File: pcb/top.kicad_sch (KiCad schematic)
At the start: 78 parts, among them J1 Conn_01x01, J10 Conn_01x01, J11 Conn_01x01, J2 Conn_01x01, J3 Conn_01x06, J4 Conn_01x01, J5 Conn_01x01, J6 Conn_01x01, J7 Conn_01x01, J8 Conn_01x01, J9 Conn_01x01, Q1 2N7002, Q2 2N7002, Q3 2N7002, Q4 2N7002, U1 L78L05_SOT89, U2 PIC12F629-ISN, U3 L78L08_SOT89

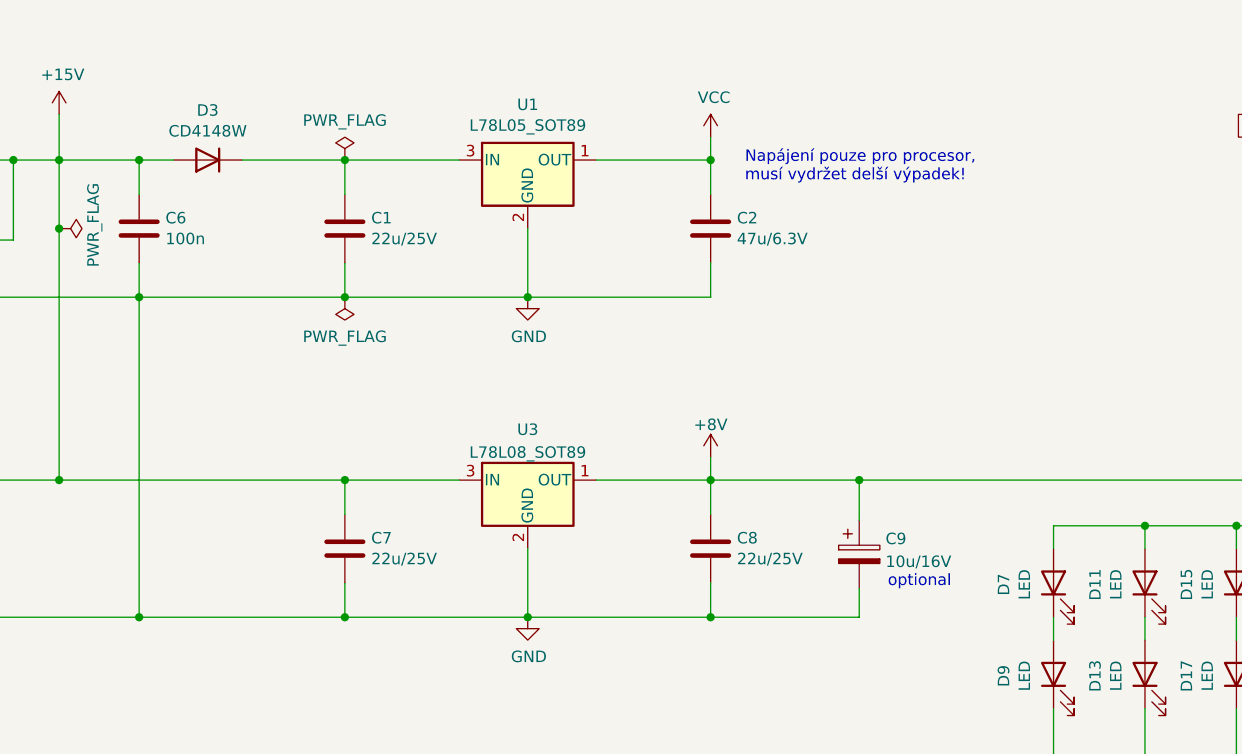
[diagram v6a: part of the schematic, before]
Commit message: Use 1N5819 insteas on 1N4148.
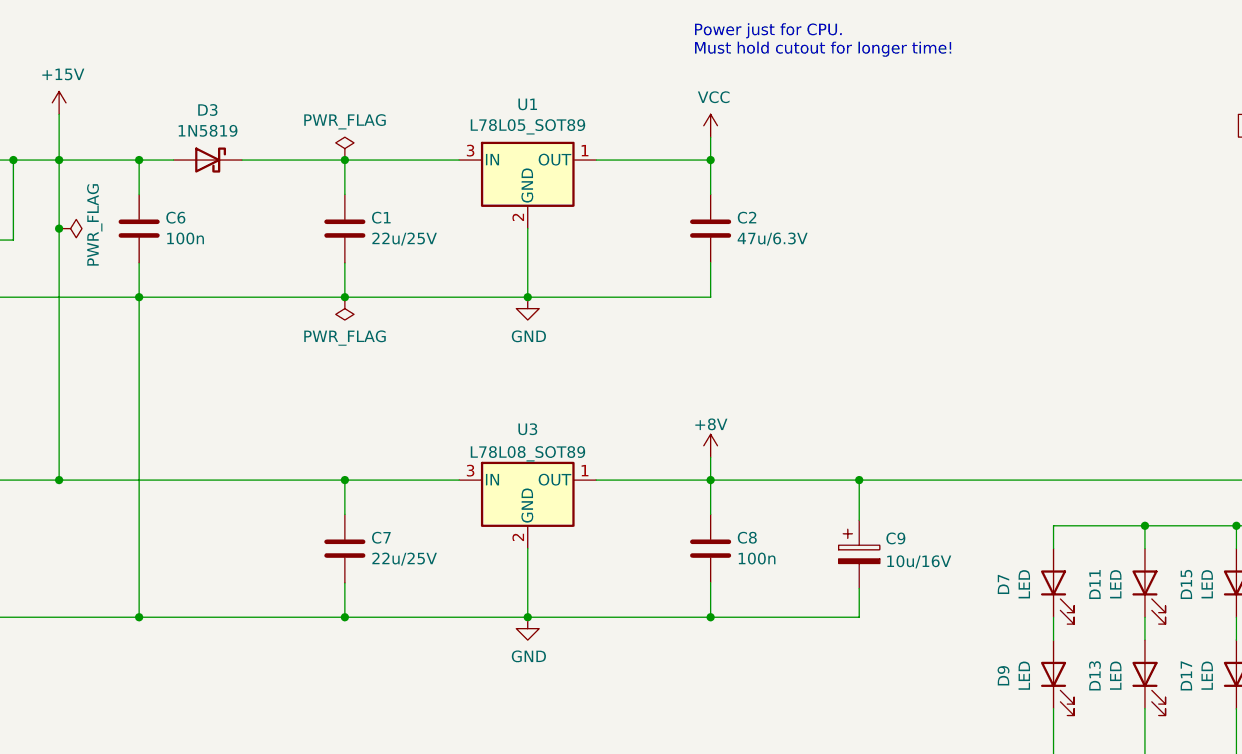
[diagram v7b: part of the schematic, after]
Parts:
- removed D3: CD4148W, Diode_SMD:D_0805_2012Metric_Pad1.15x1.40mm_HandSolder, symbol Diode:CD4148W
- added D3: 1N5819, Diode_SMD:D_SOD-123, symbol Diode:1N5819
- C8: value 22u/25V -> 100n; LCSC C45783 -> C49678
- C9: JLCPCB_IGNORE true -> (none); LCSC (none) -> C7171
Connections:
- net +15V: now also D3.2 (A)
- net at C1.1, U1.3 (IN): now also D3.1 (K)
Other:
- note added: "Power just for CPU. Must hold cutout for longer time!"
- note removed: "Napájení pouze pro procesor, musí vydržet delší výpadek!"
- note removed: "optional"
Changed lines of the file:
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@@
     (stroke (width 0) (type default) (color 0 0 0 0))
   )
-  (text "Napájení pouze pro procesor,\nmusí vydržet delší výpadek!"
-    (at 160.02 39.37 0)
+  (text "Power just for CPU.\nMust hold cutout for longer time!"
+    (at 154.305 25.4 0)
     (effects (font (size 1.27 1.27)) (justify left bottom))
   )
@@
   )
   (text "Programming\nconnector" (at 233.68 29.21 0)
-    (effects (font (size 1.27 1.27)) (justify left bottom))
-  )
-  (text "optional" (at 175.895 84.455 0)
     (effects (font (size 1.27 1.27)) (justify left bottom))
   )
@@
     (pin "2")
   )
-  (symbol (lib_id "Diode:CD4148W") (at 100.33 36.83 180) (unit 1)
-    (in_bom yes) (on_board yes)
-    (property "Reference" "D3" (id 0) (at 100.33 31.3182 0))
-    (property "Value" "CD4148W" (id 1) (at 100.33 33.6296 0))
-    (property "Footprint" "Diode_SMD:D_0805_2012Metric_Pad1.15x1.40mm_HandSolder" (id 2) (at 100.33 31.75 0)
-      (effects (font (size 1.27 1.27)) hide)
-    )
-    (property "Datasheet" "https://www.dccomponents.com/upload/product/original/806236332588.pdf" (id 3) (at 100.33 36.83 0)
-      (effects (font (size 1.27 1.27)) hide)
-    )
-    (property "LCSC" "C2128" (id 4) (at 100.33 36.83 0)
-      (effects (font (size 1.27 1.27)) hide)
-    )
-    (pin "1")
-    (pin "2")
-  )
   (symbol (lib_id "Diode:1N5819") (at 67.31 72.39 0) (mirror y) (unit 1)
     (in_bom yes) (on_board yes)
@@
       (effects (font (size 1.27 1.27)) hide)
     )
-    (property "JLCPCB_IGNORE" "true" (id 4) (at 172.72 80.645 0)
+    (property "LCSC" "C7171" (id 5) (at 172.72 80.645 0)
       (effects (font (size 1.27 1.27)) hide)
     )
@@
       (effects (font (size 1.27 1.27)) (justify left))
     )
-    (property "Value" "22u/25V" (id 1) (at 159.131 81.153 0)
+    (property "Value" "100n" (id 1) (at 159.131 81.153 0)
       (effects (font (size 1.27 1.27)) (justify left))
     )
@@
       (effects (font (size 1.27 1.27)) hide)
     )
-    (property "LCSC" "C45783" (id 4) (at 156.21 80.01 0)
+    (property "LCSC" "C49678" (id 4) (at 156.21 80.01 0)
       (effects (font (size 1.27 1.27)) hide)
     )
@@
     (pin "1")
   )
+  (symbol (lib_id "Diode:1N5819") (at 100.33 36.83 0) (mirror y) (unit 1)
+    (in_bom yes) (on_board yes)
+    (property "Reference" "D3" (id 0) (at 100.33 31.3182 0))
+    (property "Value" "1N5819" (id 1) (at 100.33 33.6296 0))
+    (property "Footprint" "Diode_SMD:D_SOD-123" (id 2) (at 100.33 41.275 0)
+      (effects (font (size 1.27 1.27)) hide)
+    )
+    (property "Datasheet" "http://www.vishay.com/docs/88525/1n5817.pdf" (id 3) (at 100.33 36.83 0)
+      (effects (font (size 1.27 1.27)) hide)
+    )
+    (property "LCSC" "C8598" (id 4) (at 100.33 36.83 0)
+      (effects (font (size 1.27 1.27)) hide)
+    )
+    (pin "1")
+    (pin "2")
+  )
   (symbol (lib_id "power:+15V") (at 261.62 110.49 0) (unit 1)
     (in_bom yes) (on_board yes)
@@
     )
     (path "/9ead4cef-69a4-4fb3-8d9a-aa12b7955333"
-      (reference "C8") (unit 1) (value "22u/25V") (footprint "Capacitor_SMD:C_0805_2012Metric_Pad1.18x1.45mm_HandSolder")
+      (reference "C8") (unit 1) (value "100n") (footprint "Capacitor_SMD:C_0805_2012Metric_Pad1.18x1.45mm_HandSolder")
     )
     (path "/802d2433-37f7-42c0-af96-9720c4dded53"
@@
       (reference "D2") (unit 1) (value "1N5819") (footprint "Diode_SMD:D_SOD-123")
     )
-    (path "/00000000-0000-0000-0000-000061ed98d7"
-      (reference "D3") (unit 1) (value "CD4148W") (footprint "Diode_SMD:D_0805_2012Metric_Pad1.15x1.40mm_HandSolder")
+    (path "/ad39d4b7-6124-465f-97ce-4b3bf28c2ece"
+      (reference "D3") (unit 1) (value "1N5819") (footprint "Diode_SMD:D_SOD-123")
     )
     (path "/00000000-0000-0000-0000-000061c6deaf"

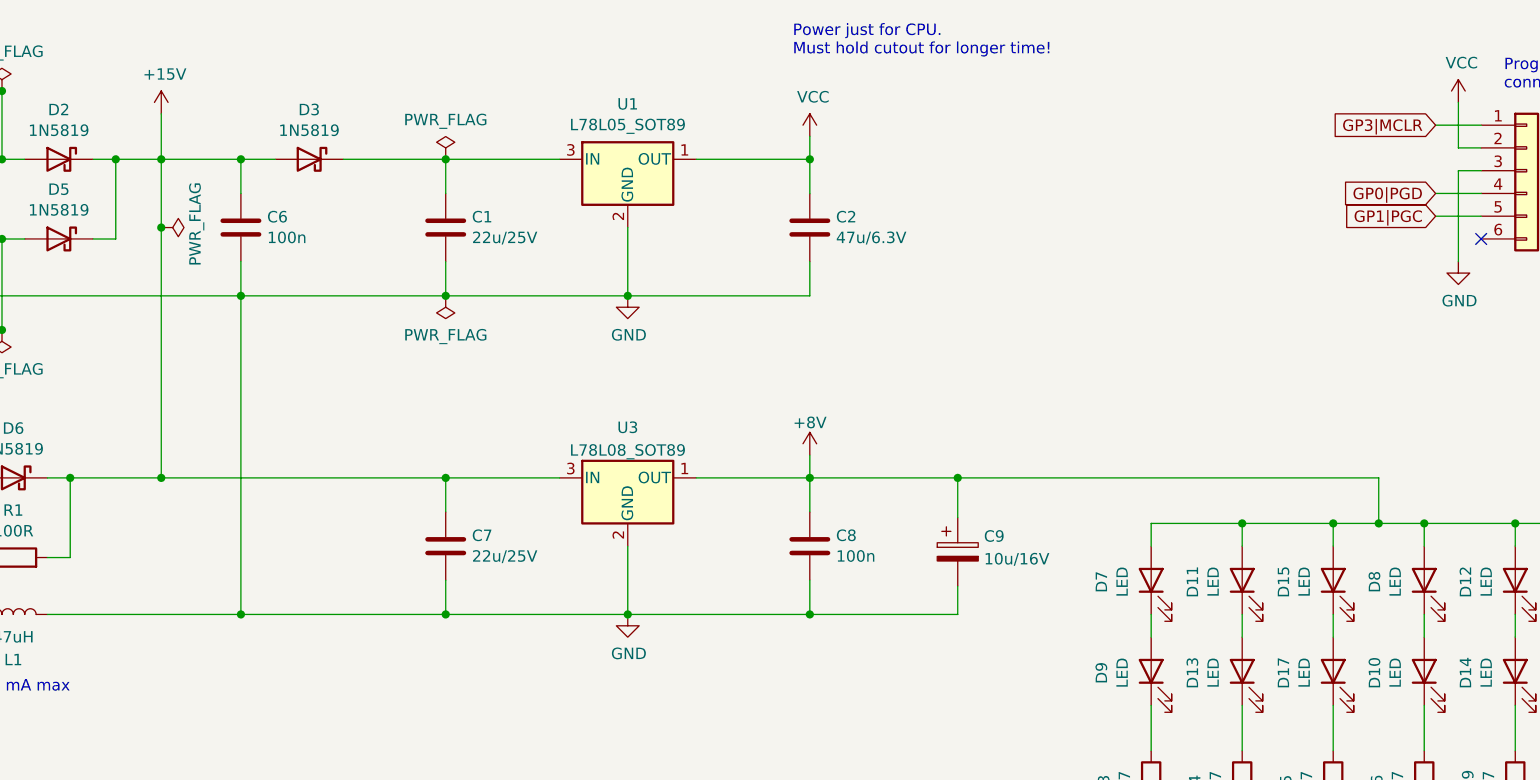
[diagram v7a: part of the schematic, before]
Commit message: Add optional tantalum capacitors.
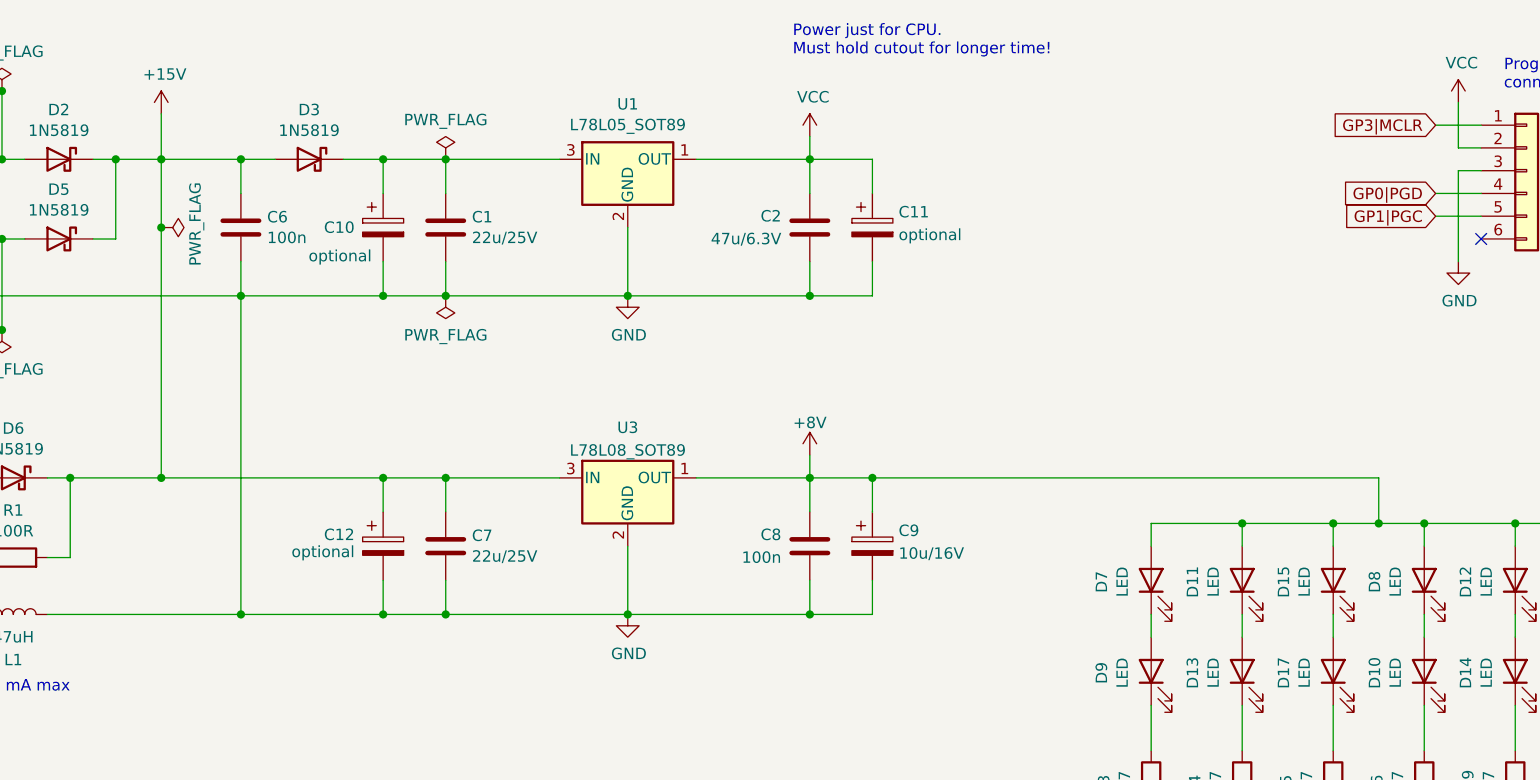
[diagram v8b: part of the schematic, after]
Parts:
- added C10, C11, C12: optional, Capacitor_Tantalum_SMD:CP_EIA-3216-10_Kemet-I, symbol Device:C_Polarized
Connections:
- net +15V: now also C12.1
- net GND: now also C10.2, C11.2, C12.2
- net VCC: now also C11.1
- net at C1.1, D3.1 (K), U1.3 (IN): now also C10.1
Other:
- moved on the sheet: C9
